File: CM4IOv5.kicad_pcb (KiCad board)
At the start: 4 copper layers, 28.5 x 44 mm, 18 parts, among them J1 Conn_01x02_Male, U1 TPD4EUSB30, U2 TPD4EUSB30, U3 MagJack-A70-112-331N126, U5 74LVC1G07SE-7

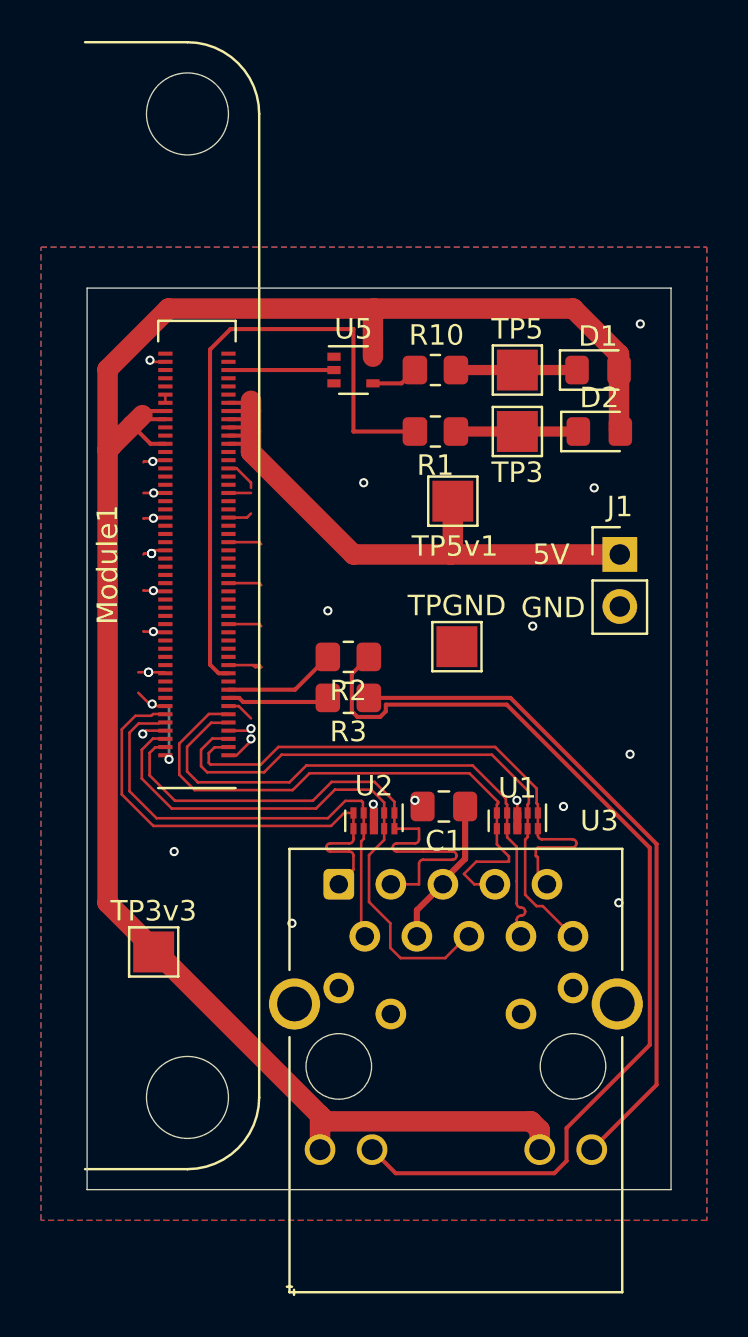
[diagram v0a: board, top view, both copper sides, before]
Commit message: Add TODO & SK6812 LED
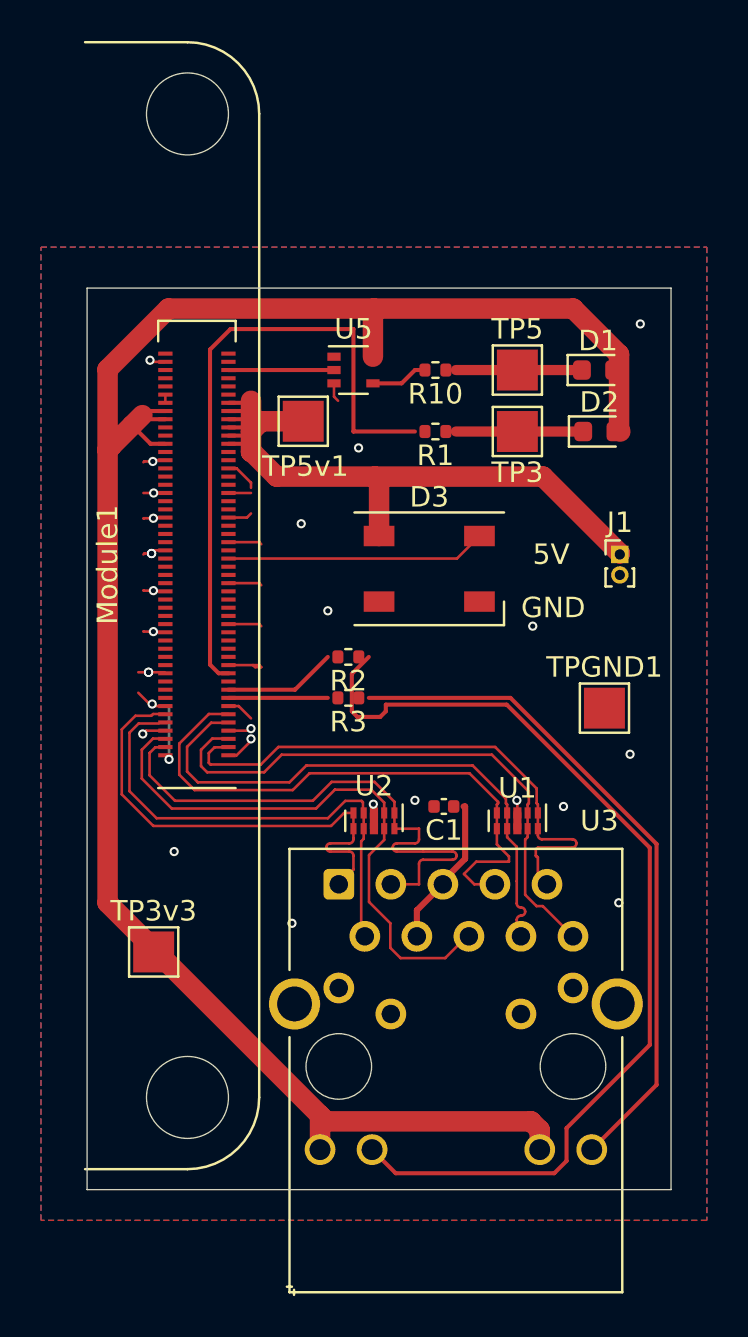
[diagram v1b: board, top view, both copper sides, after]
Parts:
- added D3: SK6812, LED_SMD:LED_SK6812_PLCC4_5.0x5.0mm_P3.2mm, F.Cu at (114.9, 101.1)
- C1: footprint Capacitor_SMD:C_0805_2012Metric_Pad1.18x1.45mm_HandSolder -> Capacitor_SMD:C_0402_1005Metric
- D1, D2: footprint LED_SMD:LED_0805_2012Metric_Pad1.15x1.40mm_HandSolder -> LED_SMD:LED_0603_1608Metric
- J1: footprint Connector_PinHeader_2.54mm:PinHeader_1x02_P2.54mm_Vertical -> Connector_PinHeader_1.00mm:PinHeader_1x02_P1.00mm_Vertical
- R1, R10, R2, R3: footprint Resistor_SMD:R_0805_2012Metric_Pad1.20x1.40mm_HandSolder -> Resistor_SMD:R_0402_1005Metric
- moved TP5v1 8.28 mm to (108.8, 93.9)
- moved TPGND1 7.80 mm to (123.5, 107.9)
- renumbered TPGND to TPGND1
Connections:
- TPGND1 pad : GND -> (no net)
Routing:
- net /CM4_GPIO ( Ethernet, GPIO, SDCARD)/GPIO18: track 0.00 -> 12.7 mm
- net /CM4_GPIO ( Ethernet, GPIO, SDCARD)/+5v: track 32.4 -> 35.4 mm
- net GND: track 32.0 -> 33.0 mm
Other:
- copper layers 4 -> 2
